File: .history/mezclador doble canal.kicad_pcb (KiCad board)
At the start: 2 copper layers, 50.8 x 60.1 mm, 31 parts, among them J1 Conn_Coaxial, J2 Conn_Coaxial, J3 Conn_Coaxial, J4 Conn_Coaxial, J5 Conn_Coaxial, J6 Conn_Coaxial, J7 Screw_Terminal_01x02, U1 NE5532

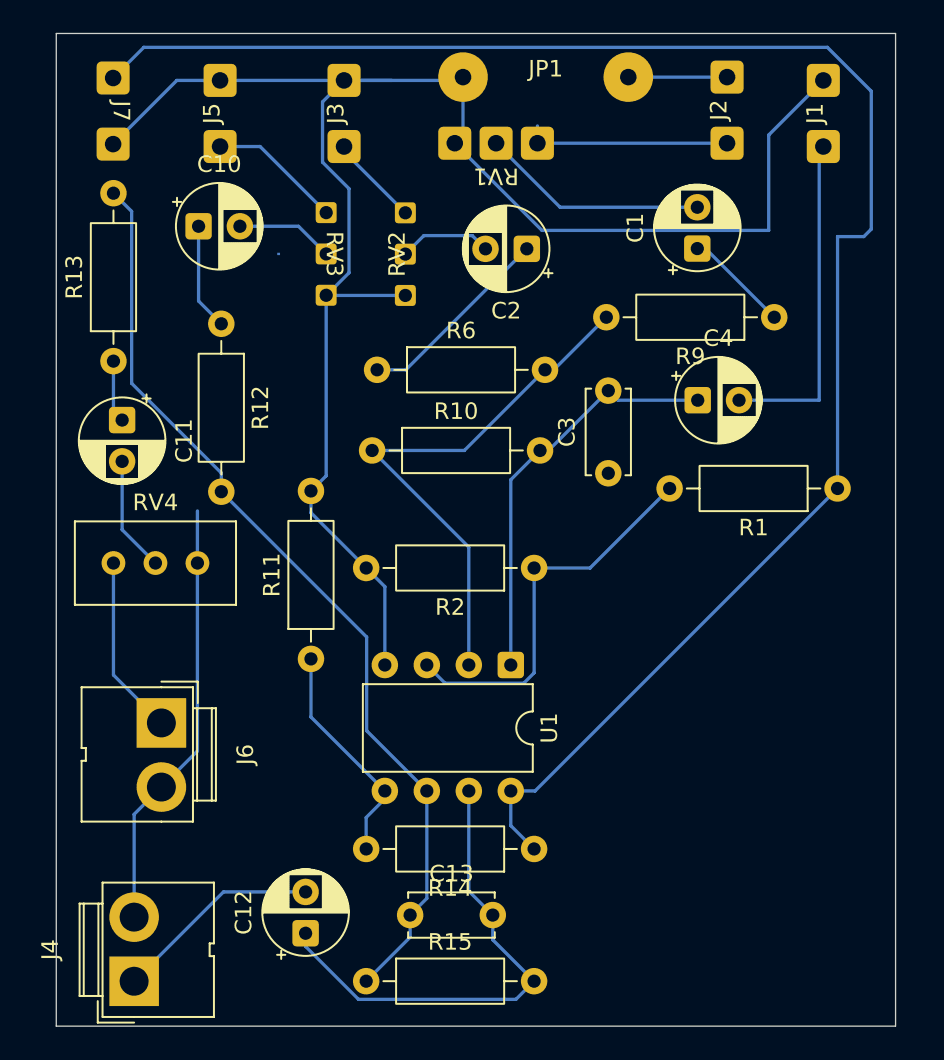
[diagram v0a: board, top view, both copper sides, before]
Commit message: mejorando distribucion de componentes
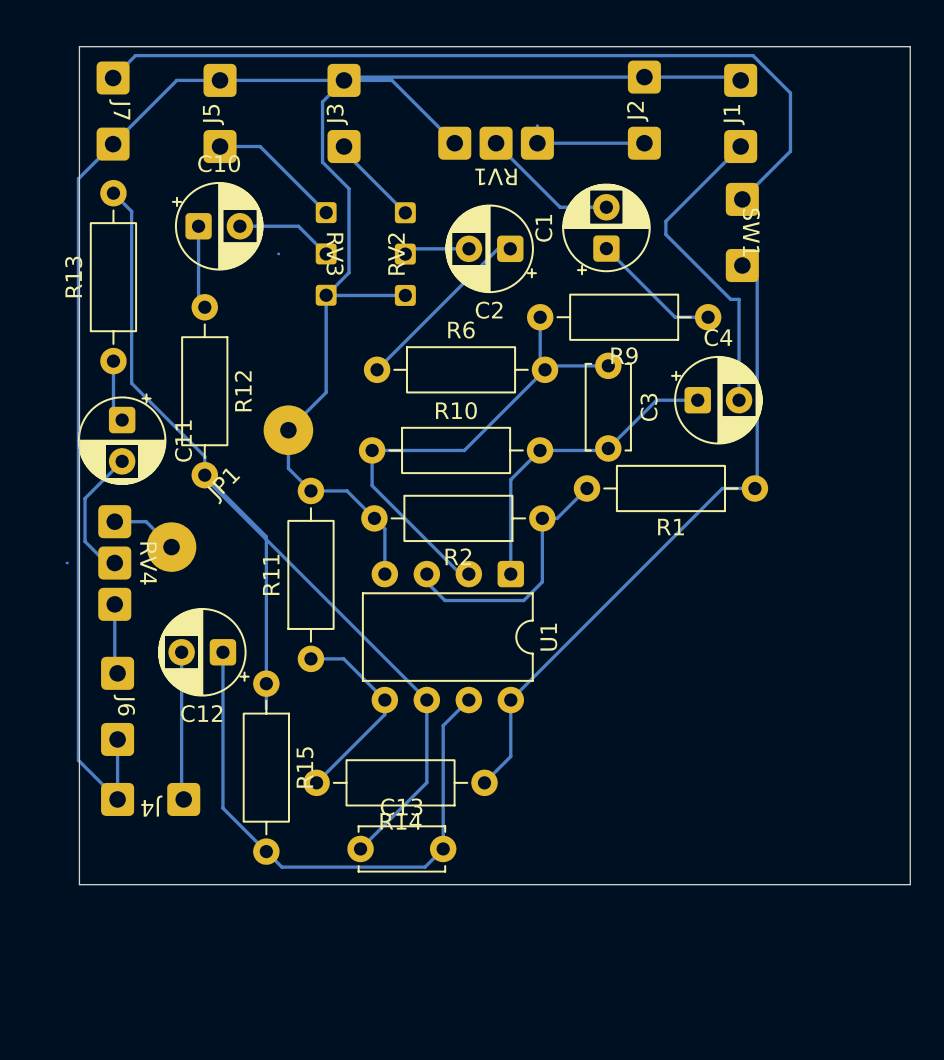
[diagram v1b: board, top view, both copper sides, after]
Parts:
- added SW1: SW_SPST, personal:double wire, F.Cu at (214.6, 57.2)
- J4, J6: footprint Connector:JWT_A3963_1x02_P3.96mm_Vertical -> personal:double wire
- RV4: footprint Potentiometer_THT:Potentiometer_Bourns_3296W_Vertical -> personal:potentiometer pads
- moved JP1 31.4 mm to (183.6, 72.7), turned to 45 degrees
- moved R15 19.0 mm to (185.8, 84.5), turned to -90 degrees
- moved C12 17.7 mm to (183.2, 82.6), turned to 180 degrees
- moved J4 11.0 mm to (178.8, 91.5), turned to 180 degrees
- moved C3 6.50 mm to (206.5, 65.3), turned to -90 degrees
- moved C1 5.50 mm to (206.4, 58.2)
- moved U1 5.50 mm to (200.6, 77.9)
- moved C13 5.00 mm to (191.5, 94.5)
- moved J1 5.00 mm to (214.5, 50.0)
- moved J2 5.00 mm to (208.7, 49.8)
- moved R1 5.00 mm to (215.4, 72.7)
- moved R14 5.00 mm to (199.0, 90.5)
- moved RV4 5.00 mm to (176.6, 77.2), turned to -90 degrees
- moved R9 4.00 mm to (212.5, 62.3)
- moved R2 3.04 mm to (202.5, 74.5)
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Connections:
- J2 pad 2: Net-(J2-Ext) -> GND
- J7 pad 1: VCC -> Net-(J7-Pin_1)
- JP1 pad 1: GND -> Net-(JP1-A)
- JP1 pad 2: Net-(J2-Ext) -> GND
- RV4 pad 1: GND -> Net-(JP1-A)
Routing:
- net VCC: track 105.0 -> 39.7 mm
- net Net-(J7-Pin_1): track 0.00 -> 50.1 mm
- net Net-(U1A-+): track 23.7 -> 15.2 mm
- net Net-(U1B--): track 57.0 -> 64.9 mm
- net Net-(J6-In): track 10.9 -> 4.25 mm
- net Net-(J2-Ext): track 5.98 -> 0.00 mm
- net Net-(C3-Pad2): track 25.0 -> 19.5 mm
- net Net-(J2-In): track 12.5 -> 7.52 mm
- net Net-(C1-Pad2): track 13.8 -> 8.78 mm
- net Net-(C12-Pad1): track 29.6 -> 34.3 mm
- net Net-(JP1-A): track 0.00 -> 4.32 mm
- net Net-(J4-In): track 12.6 -> 8.96 mm
- net GND: track 131.9 -> 135.4 mm
- net Net-(U1A--): track 32.9 -> 30.6 mm
- net Net-(C2-Pad2): track 5.65 -> 3.98 mm
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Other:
- board size 50.8 x 60.1 mm -> 50.3 x 50.7 mm

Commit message: agregando preamplificador microfono
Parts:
- added C14: C, Capacitor_THT:C_Disc_D5.0mm_W2.5mm_P5.00mm, F.Cu at (171.4, 52.8)
- added C15: C, Capacitor_THT:C_Disc_D5.0mm_W2.5mm_P5.00mm, F.Cu at (53.0, 98.0)
- added C5: C_Polarized_US, Capacitor_THT:C_Disc_D5.0mm_W2.5mm_P5.00mm, F.Cu at (96.6, 67.5)
- added J8: Conn_Coaxial, personal:double wire, F.Cu at (90.0, 75.0)
- added JP2: Jumper_2_Bridged, personal:Jumper_Wire_10mm, F.Cu at (205.4, 48.3)
- added R3: R, Resistor_THT:R_Axial_DIN0207_L6.3mm_D2.5mm_P10.16mm_Horizontal, F.Cu at (76.2, 56.5)
- added R4: R, Resistor_THT:R_Axial_DIN0207_L6.3mm_D2.5mm_P10.16mm_Horizontal, F.Cu at (80.3, 119.0)
- added R5: R, Resistor_THT:R_Axial_DIN0207_L6.3mm_D2.5mm_P10.16mm_Horizontal, F.Cu at (42.8, 118.0)
- added RV5: R_Potentiometer, personal:potentiometer pads, F.Cu at (152.4, 53.3)
- added U2: TL071, Package_DIP:DIP-8_W7.62mm, F.Cu at (53.3, 25.4)
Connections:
- RV1 pad 1: Net-(J2-In) -> Net-(JP2-B)
- RV4 pad 3: Net-(J6-In) -> Net-(JP2-A)
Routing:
- net Net-(JP2-A): track 0.00 -> 95.0 mm
- net Net-(JP2-B): track 0.00 -> 3.75 mm
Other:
- board outline removed

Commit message: acomodando componentes
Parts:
- moved U2 103.2 mm to (154.1, 47.7)
- moved R3 94.7 mm to (169.9, 69.9)
- moved SW1 24.7 mm to (208.2, 81.0)
- moved R1 21.5 mm to (203.8, 90.8), turned to 90 degrees
- moved J1 18.4 mm to (210.3, 68.0)
- moved C13 17.0 mm to (208.2, 91.3), turned to 90 degrees
- moved RV5 15.2 mm to (167.3, 50.1)
- moved C4 9.53 mm to (205.7, 74.5)
- moved R15 4.28 mm to (185.7, 80.2)
- moved R9 2.15 mm to (210.4, 62.3)
- moved C2 0.54 mm to (200.0, 58.2)
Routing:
- net Net-(C12-Pad1): track 34.3 -> 59.1 mm
- net Net-(J7-Pin_1): track 50.1 -> 71.7 mm
- net VCC: track 39.7 -> 19.2 mm
- net GND: track 135.4 -> 149.3 mm
- net Net-(J1-In): track 19.4 -> 5.49 mm
- net Net-(C1-Pad1): track 7.88 -> 5.81 mm
- net Net-(C3-Pad2): track 19.5 -> 17.5 mm
- net Net-(U1B--): track 64.9 -> 66.4 mm
- net Net-(U1A--): track 30.6 -> 31.5 mm
- net Net-(U1A-+): track 15.2 -> 16.0 mm
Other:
- board outline added: 50.2 x 50.3 mm

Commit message: acomodando componentes
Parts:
- added D1: LED, LED_THT:LED_D5.0mm, F.Cu at (211.7, 79.8)
- added JP3: Jumper_2_Bridged, personal:Jumper_Wire_7mm, F.Cu at (177.6, 46.5)
- added R7: R, Resistor_THT:R_Axial_DIN0207_L6.3mm_D2.5mm_P7.62mm_Horizontal, F.Cu at (211.8, 92.2)
- JP2: footprint personal:Jumper_Wire_10mm -> personal:Jumper_Wire_7mm
- moved R5 134.2 mm to (165.9, 64.5), turned to -90 degrees
- moved C15 117.9 mm to (163.7, 57.4), turned to -90 degrees
- moved R4 85.7 mm to (161.5, 91.5), turned to 0 degrees
- moved J8 78.0 mm to (163.7, 49.6), turned to 90 degrees
- moved C5 74.7 mm to (171.3, 70.0), turned to -90 degrees
- moved U2 42.0 mm to (168.9, 87.0), turned to 180 degrees
- moved R3 3.13 mm to (171.3, 67.1)
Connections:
- J8 pad 2: GND -> Net-(J8-Ext)
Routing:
- net VCC: track 19.2 -> 70.1 mm
- net GND: track 149.3 -> 170.4 mm
- net Net-(J8-Ext): track 0.00 -> 12.1 mm
- net Net-(U2--): track 0.00 -> 10.9 mm
- net Net-(JP2-A): track 95.0 -> 101.0 mm
- net Net-(JP2-B): track 3.75 -> 0.17 mm
- net Net-(C5-Pad1): track 0.00 -> 2.86 mm
- net Net-(D1-A): track 0.00 -> 2.33 mm
- net Net-(J2-In): track 7.52 -> 6.48 mm
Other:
- board size 50.2 x 50.3 mm -> 53.4 x 51.5 mm

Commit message: todos los componentes enrutadosgit add .!
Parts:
- removed J6: Conn_Coaxial, personal:double wire
- moved C5 8.00 mm to (171.3, 62.0), turned to 90 degrees
- moved J4 4.00 mm to (178.8, 87.5)
- moved R3 2.00 mm to (171.3, 65.1), turned to -90 degrees
- moved C15 1.00 mm to (163.7, 56.4)
- moved U2 1.00 mm to (169.9, 87.0)
- moved R4 0.50 mm to (162.0, 91.5)
- moved R5 0.50 mm to (165.9, 65.0)
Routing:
- net GND: track 170.4 -> 294.6 mm
- net VCC: track 70.1 -> 116.1 mm
- net Net-(U2--): track 10.9 -> 42.5 mm
- net Net-(U2-+): track 0.00 -> 21.2 mm
- net Net-(JP2-A): track 101.0 -> 117.5 mm
- net Net-(J8-In): track 0.00 -> 9.82 mm
- net Net-(J6-In): track 4.25 -> 0.00 mm
- net Net-(J4-In): track 8.96 -> 4.96 mm
- net Net-(C5-Pad1): track 2.86 -> 0.00 mm
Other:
- board size 53.4 x 51.5 mm -> 55 x 54 mm

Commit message: todo en su lugar / tamaño 50x55
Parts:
- removed J2: Conn_Coaxial, personal:double wire
- removed JP1: Jumper_2_Bridged, personal:Jumper_Wire_10mm
- removed JP2, JP3: Jumper_2_Bridged, personal:Jumper_Wire_7mm
- moved C12 1.00 mm to (182.2, 82.6)
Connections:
- C14 pad 2: Net-(JP2-A) -> Net-(C14-Pad2)
- J8 pad 2: Net-(J8-Ext) -> GND
- RV1 pad 1: Net-(JP2-B) -> Net-(C14-Pad2)
- RV4 pad 1: Net-(JP1-A) -> GND
- RV4 pad 3: Net-(JP2-A) -> Net-(C14-Pad2)
- RV5 pad 3: Net-(JP2-A) -> Net-(C14-Pad2)
- U2 pad 6: Net-(JP2-A) -> Net-(C14-Pad2)
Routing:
- net Net-(JP2-A): track 117.5 -> 0.00 mm
- net Net-(C14-Pad2): track 0.00 -> 116.5 mm
- net GND: track 294.6 -> 330.7 mm
- net Net-(C12-Pad1): track 59.1 -> 35.0 mm
- net Net-(J8-Ext): track 12.1 -> 0.00 mm
- net Net-(J2-In): track 6.48 -> 0.00 mm
- net Net-(JP1-A): track 4.32 -> 0.00 mm
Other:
- board size 55 x 54 mm -> 55 x 50.1 mm

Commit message: todo acomodado - corregir etiquetas
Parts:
- D1: footprint LED_THT:LED_D5.0mm -> personal:double wire
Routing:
- net GND: track 330.7 -> 334.8 mm
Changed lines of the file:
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@@
 		)
 	)
-	(footprint "LED_THT:LED_D5.0mm"
+	(footprint "personal:double wire"
 		(layer "F.Cu")
 		(at 211.65 79.75 -90)
-		(descr "LED, diameter 5.0mm, 2 pins, http://cdn-reichelt.de/documents/datenblatt/A500/LL-504BC2E-009.pdf, generated by kicad-footprint-generator")
-		(tags "LED")
 		(property "Reference" "D1"
-			(at 1.27 -3.96 90)
+			(at 0 -0.5 270)
+			(unlocked yes)
 			(layer "F.SilkS")
 			(effects
 				(font
 					(size 1 1)
-					(thickness 0.15)
+					(thickness 0.1)
 				)
 			)
 		)
 		(property "Value" "LED"
-			(at 1.27 3.96 90)
+			(at 0 1 270)
+			(unlocked yes)
 			(layer "F.Fab")
 			(effects
@@
 		)
 		(property "Datasheet" ""
-			(at 0 0 90)
+			(at 0 0 270)
+			(unlocked yes)
 			(layer "F.Fab")
 			(hide yes)
 			(effects
 				(font
-					(size 1.27 1.27)
+					(size 1 1)
+					(thickness 0.15)
 				)
 			)
 		)
 		(property "Description" "Light emitting diode"
-			(at 0 0 90)
+			(at 0 0 270)
+			(unlocked yes)
 			(layer "F.Fab")
 			(hide yes)
 			(effects
 				(font
-					(size 1.27 1.27)
-				)
-			)
-		)
-		(property "KiLib_Generator" "LED/THT"
-			(at 0 0 90)
-			(layer "F.SilkS")
-			(hide yes)
-			(effects
-				(font
 					(size 1 1)
 					(thickness 0.15)
@@
 			)
 		)
-		(attr through_hole)
+		(attr smd)
 		(duplicate_pad_numbers_are_jumpers no)
-		(fp_line
-			(start -1.29 -1.545)
-			(end -1.29 1.545)
-			(stroke
-				(width 0.12)
-				(type solid)
-			)
-			(layer "F.SilkS")
-		)
-		(fp_arc
-			(start 4.26 0)
-			(mid 2.071779 2.880495)
-			(end -1.29 1.54483)
-			(stroke
-				(width 0.12)
-				(type solid)
-			)
-			(layer "F.SilkS")
-		)
-		(fp_arc
-			(start -1.29 -1.54483)
-			(mid 2.071779 -2.880495)
-			(end 4.26 0)
-			(stroke
-				(width 0.12)
-				(type solid)
-			)
-			(layer "F.SilkS")
-		)
-		(fp_circle
-			(center 1.27 0)
-			(end 3.77 0)
-			(stroke
-				(width 0.12)
-				(type solid)
-			)
-			(fill no)
-			(layer "F.SilkS")
-		)
-		(fp_rect
-			(start -1.94 -3.21)
-			(end 4.49 3.21)
-			(stroke
-				(width 0.05)
-				(type solid)
-			)
-			(fill no)
-			(layer "F.CrtYd")
-		)
-		(fp_line
-			(start -1.23 -1.469694)
-			(end -1.23 1.469694)
-			(stroke
-				(width 0.1)
-				(type solid)
-			)
-			(layer "F.Fab")
-		)
-		(fp_arc
-			(start -1.23 -1.469694)
-			(mid 4.17 0)
-			(end -1.23 1.469694)
-			(stroke
-				(width 0.1)
-				(type solid)
-			)
-			(layer "F.Fab")
-		)
-		(fp_circle
-			(center 1.27 0)
-			(end 3.77 0)
-			(stroke
-				(width 0.1)
-				(type solid)
-			)
-			(fill no)
-			(layer "F.Fab")
-		)
-		(fp_text user "${REFERENCE}"
-			(at 1.27 0 90)
+		(fp_text user "."
+			(at 0 2.5 270)
+			(unlocked yes)
 			(layer "F.Fab")
 			(effects
 				(font
-					(size 0.8 0.8)
-					(thickness 0.12)
+					(size 1 1)
+					(thickness 0.15)
 				)
 			)
 		)
-		(point
-			(at 211.65 81.02)
-			(size 2)
-			(layer "F.Fab")
-		)
-		(pad "1" thru_hole rect
-			(at 0 0 270)
-			(size 1.8 1.8)
-			(drill 0.9)
+		(pad "1" thru_hole roundrect
+			(at -2 0 270)
+			(size 2 2)
+			(drill 1)
 			(layers "*.Cu" "*.Mask")
 			(remove_unused_layers no)
+			(roundrect_rratio 0.15)
 			(net "GND")
 			(pinfunction "K_1")
 			(pintype "passive")
 		)
-		(pad "2" thru_hole circle
-			(at 2.54 0 270)
-			(size 1.8 1.8)
-			(drill 0.9)
+		(pad "2" thru_hole roundrect
+			(at 2 0 270)
+			(size 2 2)
+			(drill 1)
 			(layers "*.Cu" "*.Mask")
 			(remove_unused_layers no)
+			(roundrect_rratio 0.15)
 			(net "Net-(D1-A)")
 			(pinfunction "A_2")
@@
 		)
 		(embedded_fonts no)
-		(model "${KICAD10_3DMODEL_DIR}/LED_THT.3dshapes/LED_D5.0mm.step"
-			(offset
-				(xyz 0 0 0)
-			)
-			(scale
-				(xyz 1 1 1)
-			)
-			(rotate
-				(xyz 0 0 0)
-			)
-		)
 	)
 	(footprint "Capacitor_THT:CP_Radial_D5.0mm_P2.50mm"
@@
 	)
 	(segment
+		(start 212.95 92.555635)
+		(end 212.95 79.05)
+		(width 0.2)
+		(layer "B.Cu")
+		(net "GND")
+	)
+	(segment
 		(start 174.43 85.135)
 		(end 176.8 87.505)
@@
 	)
 	(segment
-		(start 160.1 60)
-		(end 160.1 94.325)
-		(width 0.2)
-		(layer "B.Cu")
-		(net "GND")
-	)
-	(segment
-		(start 211.180635 94.325)
-		(end 160.1 94.325)
-		(width 0.2)
-		(layer "B.Cu")
-		(net "GND")
-	)
-	(segment
-		(start 212.85 80.95)
-		(end 212.85 92.655635)
+		(start 209.7 80.699999)
+		(end 209.7 81.7)
 		(width 0.2)
 		(layer "B.Cu")
@@
 	)
 	(segment
+		(start 160.1 60)
+		(end 160.1 94.325)
+		(width 0.2)
+		(layer "B.Cu")
+		(net "GND")
+	)
+	(segment
 		(start 196.8 81.7)
 		(end 209.7 81.7)
@@
 	)
 	(segment
+		(start 160.1 94.325)
+		(end 211.180635 94.325)
+		(width 0.2)
+		(layer "B.Cu")
+		(net "GND")
+	)
+	(segment
 		(start 190.68 72.84)
 		(end 192.34 74.5)
@@
 	)
 	(segment
-		(start 176.63 74.7)
-		(end 176.63 74.95147)
+		(start 212.95 79.05)
+		(end 211.65 77.75)
 		(width 0.2)
 		(layer "B.Cu")
@@
 	)
 	(segment
-		(start 211.65 79.75)
-		(end 212.85 80.95)
-		(width 0.2)
-		(layer "B.Cu")
-		(net "GND")
-	)
-	(segment
-		(start 212.85 92.655635)
-		(end 211.180635 94.325)
+		(start 176.63 74.7)
+		(end 176.63 74.95147)
 		(width 0.2)
 		(layer "B.Cu")
@@
 	)
 	(segment
-		(start 209.7 81.7)
-		(end 211.65 79.75)
+		(start 189.42 61)
+		(end 189.42 66.88)
 		(width 0.2)
 		(layer "B.Cu")
@@
 	)
 	(segment
-		(start 189.42 61)
-		(end 189.42 66.88)
+		(start 163.7 56.4)
+		(end 160.1 60)
 		(width 0.2)
 		(layer "B.Cu")
@@
 	)
 	(segment
+		(start 211.65 78.749999)
+		(end 209.7 80.699999)
+		(width 0.2)
+		(layer "B.Cu")
+		(net "GND")
+	)
+	(segment
 		(start 190.5 48)
 		(end 193.4 48)
@@
 	)
 	(segment
+		(start 211.65 77.75)
+		(end 211.65 78.749999)
+		(width 0.2)
+		(layer "B.Cu")
+		(net "GND")
+	)
+	(segment
+		(start 211.180635 94.325)
+		(end 212.95 92.555635)
+		(width 0.2)
+		(layer "B.Cu")
+		(net "GND")
+	)
+	(segment
 		(start 192.97 77.87)
 		(end 196.8 81.7)
@@
 	)
 	(segment
-		(start 163.7 56.4)
-		(end 160.1 60)
-		(width 0.2)
-		(layer "B.Cu")
-		(net "GND")
-	)
-	(segment
 		(start 165.9 75.21)
 		(end 165.9 77.92)
@@
 	)
 	(segment
-		(start 212.375 76.675)
-		(end 209.325 79.725)
+		(start 208.9 79.725)
+		(end 208.225 79.05)
 		(width 0.2)
 		(layer "B.Cu")
@@
 	)
 	(segment
-		(start 208.9 79.725)
+		(start 208.225 76.030635)
 		(end 208.225 79.05)
 		(width 0.2)
@@
 	(segment
 		(start 212.375 48.125)
-		(end 212.375 76.675)
+		(end 212.375 71.880635)
 		(width 0.2)
 		(layer "B.Cu")
@@
 		(width 0.2)
 		(layer "B.Cu")
+		(net "Net-(J7-Pin_1)")
+	)
+	(segment
+		(start 212.375 71.880635)
+		(end 208.225 76.030635)
+		(width 0.2)
+		(layer "B.Cu")

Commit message: depurando proyecto
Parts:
- R2: renamed from R3; value R -> R2
- renumbered C5 to C1, C12 to C10, C13 to C11, C14 to C2, C1 to C3, C2 to C4, C10 to C5, C11 to C6, C4 to C7, C3 to C8, C15 to C9, R4 to R1, R13 to R10, R14 to R11, R11 to R12, R15 to R13, R7 to R14, R5 to R3, R9 to R4, R6 to R5, R1 to R6, R2 to R7, R10 to R8, R12 to R9
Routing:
- net Net-(C1-Pad1): track 0.00 -> 3.18 mm
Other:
- board text added: "nestitormdq@gmail.com"
